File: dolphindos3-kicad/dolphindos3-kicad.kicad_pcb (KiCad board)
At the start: 2 copper layers, 23 parts, among them CN1 MB_CPU, CN2 parallel0, IC1 6502, IC10 74LS08, IC2 27256, IC3 6264, IC4 6821, IC5 74LS08, IC6 74LS08, IC7 74LS32, IC8 74LS04, IC9 74LS32

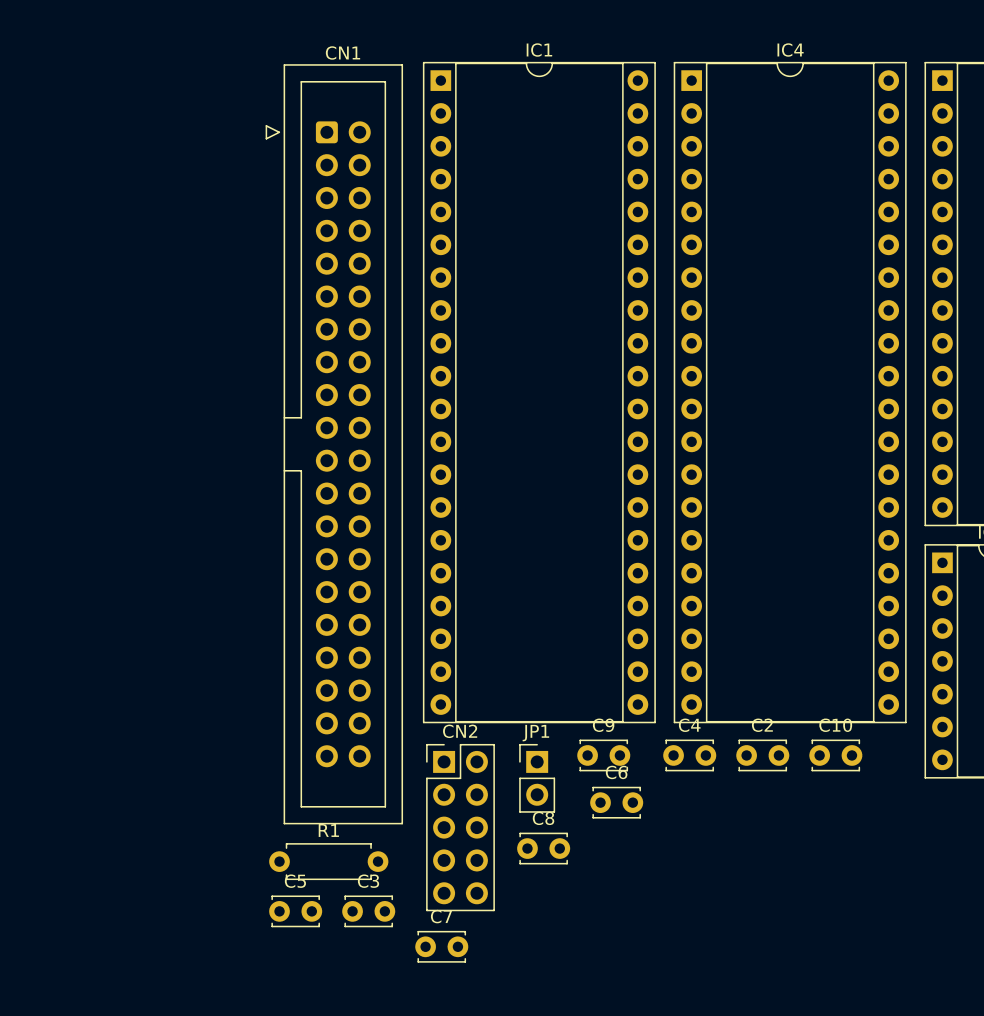
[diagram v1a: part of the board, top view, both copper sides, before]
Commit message: IDC socket for parallel cable, added JP2 for drive reset to match gerbers
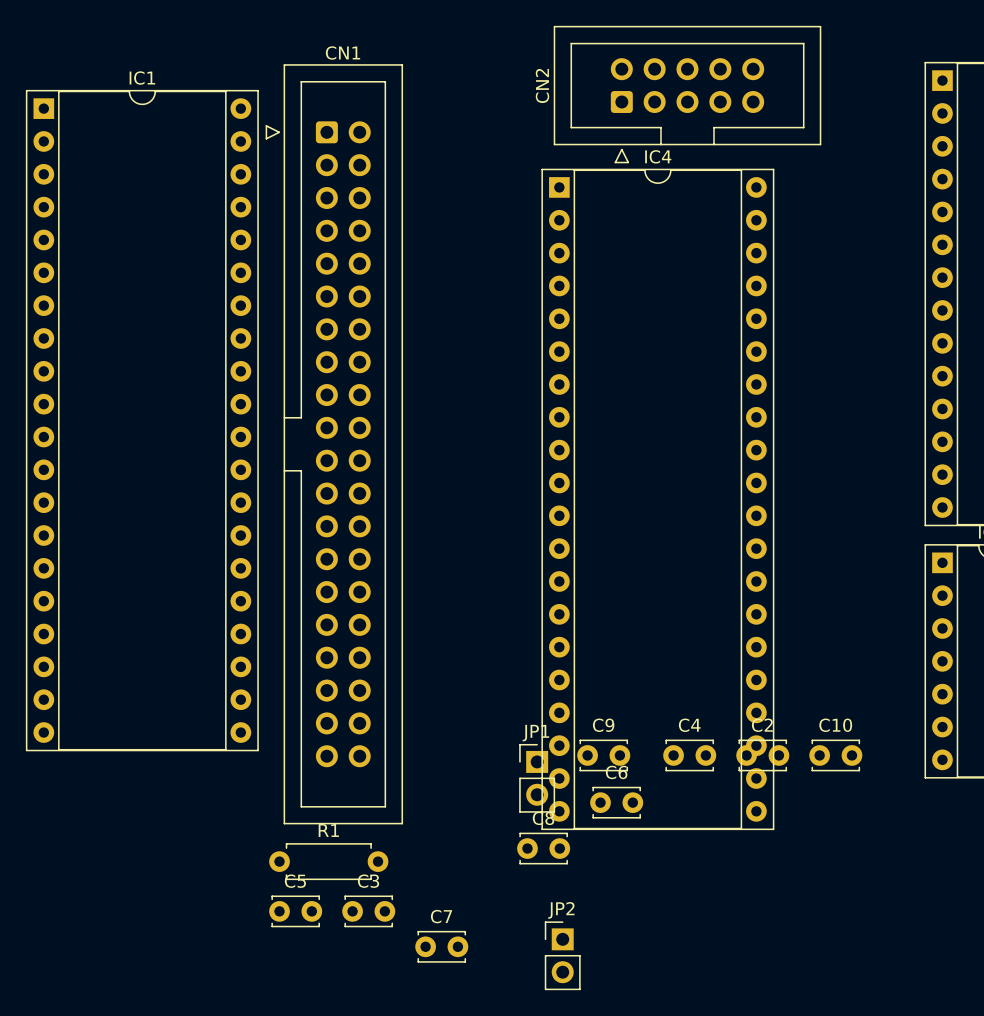
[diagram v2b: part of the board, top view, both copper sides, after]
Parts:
- added JP2: Conn_01x02, Connector_PinHeader_2.54mm:PinHeader_1x02_P2.54mm_Vertical, F.Cu at (190.2, 84.3)
- CN2: footprint Connector_PinHeader_2.54mm:PinHeader_2x05_P2.54mm_Vertical -> Connector_IDC:IDC-Header_2x05_P2.54mm_Vertical
- moved CN2 52.9 mm to (194.8, 19.6), turned to 90 degrees
- moved IC1 30.8 mm to (150.1, 20.1)
- moved IC4 13.2 mm to (190.0, 26.2)

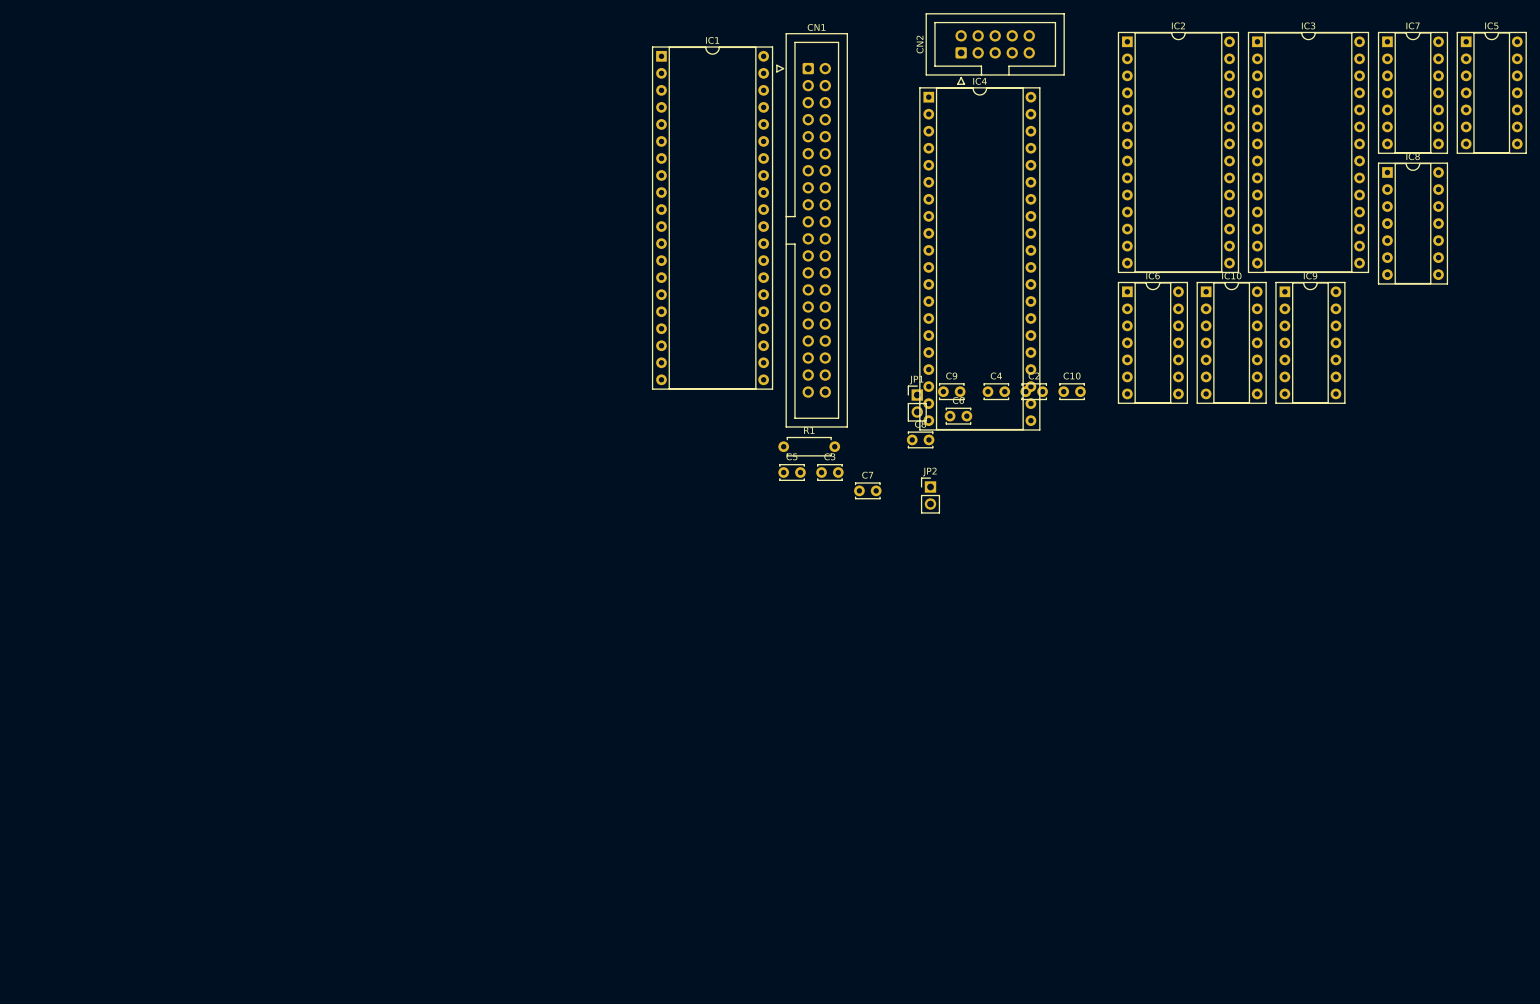
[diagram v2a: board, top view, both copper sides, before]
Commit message: F.Cu, B.Cu and F.Silkscreen copied from SliverDreams! rev2a gerber files, Edge.cuts eyeballed; placed parts and added footprints
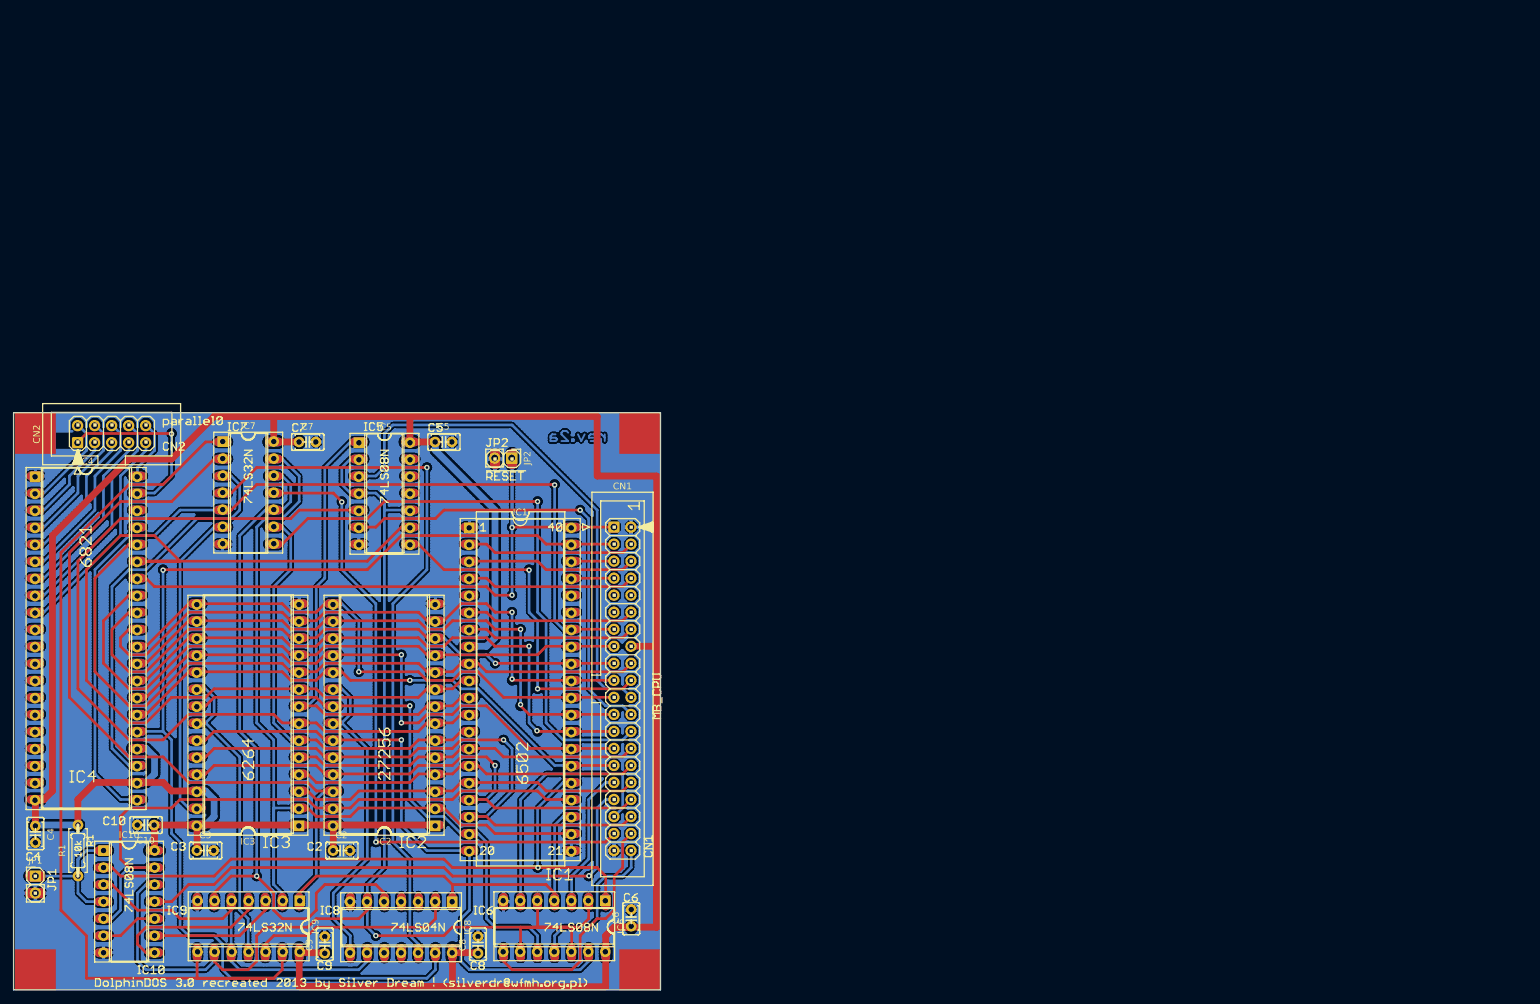
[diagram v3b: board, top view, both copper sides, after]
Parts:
- moved IC3 184.8 mm to (96.0, 134.9), turned to 180 degrees
- moved IC10 184.4 mm to (66.9, 138.6)
- moved IC7 183.7 mm to (84.6, 77.5)
- moved IC8 176.9 mm to (118.9, 146.2), turned to -90 degrees
- moved IC5 175.7 mm to (105.0, 77.7)
- moved IC9 172.8 mm to (96.1, 146.1), turned to -90 degrees
- moved C4 156.2 mm to (56.7, 134.9), turned to -90 degrees
- moved IC2 156.1 mm to (116.3, 134.9), turned to 180 degrees
- moved C10 150.3 mm to (74.4, 134.8), turned to 180 degrees
- moved JP1 149.9 mm to (56.7, 142.4)
- moved IC4 144.9 mm to (56.6, 82.8)
- moved CN2 144.1 mm to (63.0, 77.7)
- moved C9 124.7 mm to (99.9, 153.9), turned to 90 degrees
- moved C2 124.0 mm to (101.1, 138.6)
- moved R1 123.2 mm to (63.1, 142.4), turned to 90 degrees
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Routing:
- net GND: track 0.00 -> 16178.4 mm
- net VCC: track 0.00 -> 610.9 mm
- net Net-(IC10-Pad12): track 0.00 -> 230.4 mm, vias 0 -> 1
- net /A13: track 0.00 -> 190.4 mm
- net /phi2: track 0.00 -> 182.6 mm, vias 0 -> 1
- net /A1: track 0.00 -> 159.9 mm
- net Net-(IC7-Pad1): track 0.00 -> 151.5 mm
- net /R/~{W}: track 0.00 -> 149.9 mm, vias 0 -> 1
- net /A12: track 0.00 -> 145.8 mm
- net /A3: track 0.00 -> 139.9 mm
- net /A0: track 0.00 -> 120.9 mm
- net Net-(IC7-Pad10): track 0.00 -> 115.0 mm, vias 0 -> 1
- net /A15: track 0.00 -> 113.7 mm, vias 0 -> 1
- net Net-(IC7-Pad4): track 0.00 -> 113.4 mm, vias 0 -> 1
- net /~{RESET}: track 0.00 -> 108.1 mm, vias 0 -> 2
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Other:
- board outline added: 96.5 x 86.1 mm

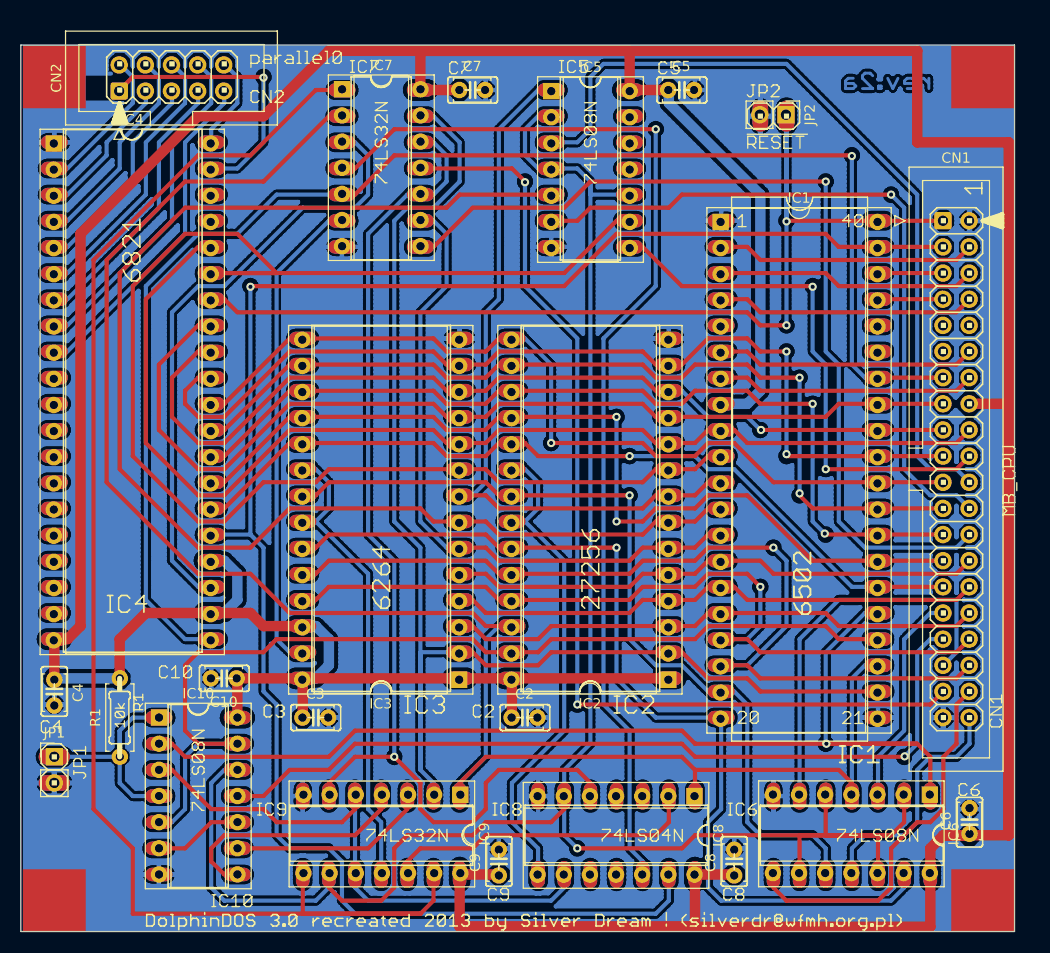
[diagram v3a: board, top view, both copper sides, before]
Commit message: mods: RAM A13/14 from PIA PB, ROM A15, unused gate inputs tied to GND pcb: autorouted, parts moved for C128DCR plug-in option
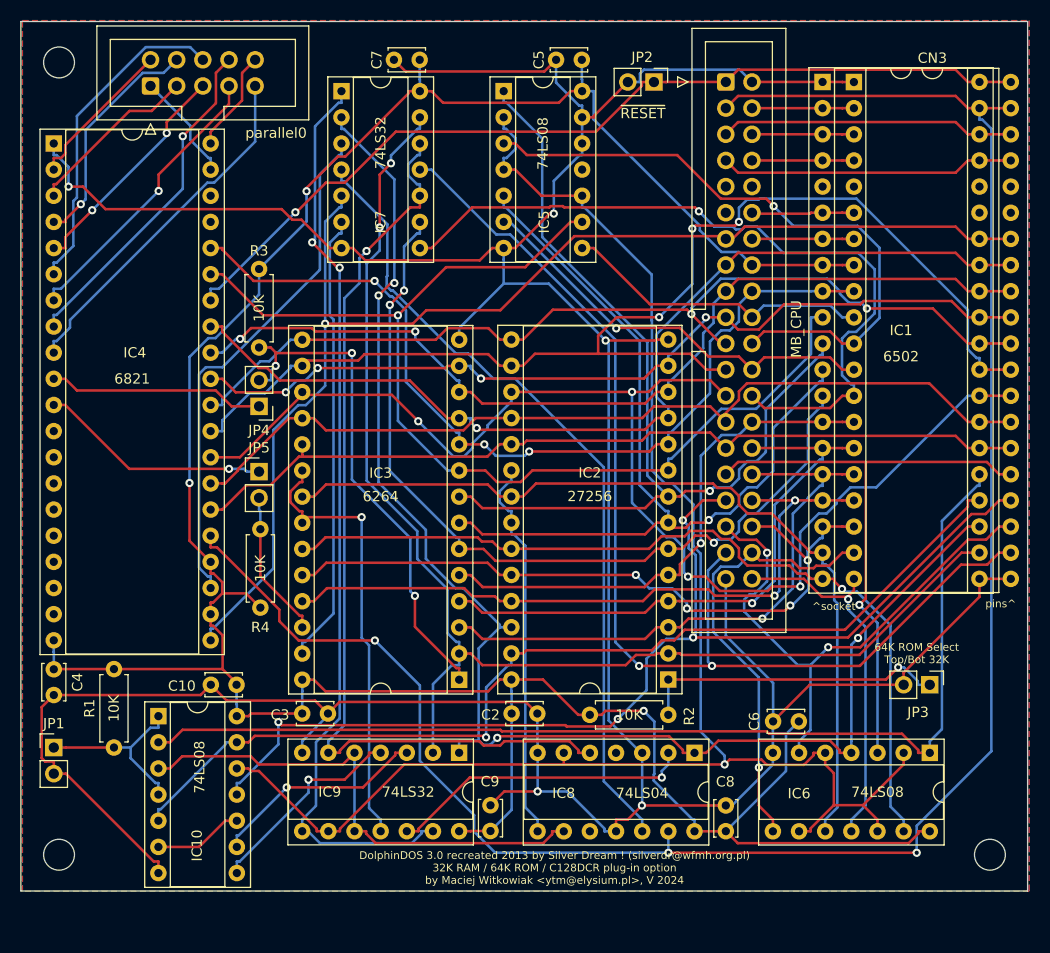
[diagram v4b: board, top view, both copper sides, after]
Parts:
- added CN3: MB_CPU_PINS, Package_DIP:DIP-40_W15.24mm, F.Cu at (134.4, 76.8)
- added H1: MountingHole, MountingHole:MountingHole_3mm, F.Cu at (57.1, 74.9)
- added H3: MountingHole, MountingHole:MountingHole_3mm, F.Cu at (57.1, 151.9)
- added H4: MountingHole, MountingHole:MountingHole_3mm, F.Cu at (147.6, 151.9)
- added JP3: Conn_01x02, Connector_PinHeader_2.54mm:PinHeader_1x02_P2.54mm_Vertical, F.Cu at (141.7, 135.4)
- added JP4: Jumper_2_Open, Connector_PinHeader_2.54mm:PinHeader_1x02_P2.54mm_Vertical, F.Cu at (76.6, 108.3)
- added JP5: Jumper_2_Open, Connector_PinHeader_2.54mm:PinHeader_1x02_P2.54mm_Vertical, F.Cu at (76.6, 114.7)
- added R2: 10K, Resistor_THT:R_Axial_DIN0207_L6.3mm_D2.5mm_P7.62mm_Horizontal, F.Cu at (116.3, 138.3)
- added R3: 10K, Resistor_THT:R_Axial_DIN0207_L6.3mm_D2.5mm_P7.62mm_Horizontal, F.Cu at (76.6, 95.0)
- added R4: 10K, Resistor_THT:R_Axial_DIN0207_L6.3mm_D2.5mm_P7.62mm_Horizontal, F.Cu at (76.7, 127.9)
- moved CN1 25.0 mm to (121.9, 76.8)
- moved C6 19.9 mm to (129.0, 138.9), turned to 180 degrees
- moved IC1 16.8 mm to (131.3, 76.8)
- moved JP2 13.2 mm to (114.9, 76.8)
- moved C5 8.90 mm to (107.9, 74.7), turned to 180 degrees
- moved C7 4.84 mm to (92.2, 74.7), turned to 180 degrees
- moved IC5 4.62 mm to (100.3, 77.7)
- moved C9 4.39 mm to (99.1, 149.6)
- moved C8 4.37 mm to (121.9, 149.6)
- moved IC8 4.20 mm to (118.9, 142.0)
- moved IC9 4.08 mm to (96.0, 142.0)
- moved IC6 4.05 mm to (141.7, 142.0)
- moved CN2 3.09 mm to (66.0, 77.2)
- moved R1 1.06 mm to (62.5, 141.5)
- moved C4 1.02 mm to (56.6, 133.9)
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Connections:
- IC2 pad 1: VCC -> Net-(IC2-Pad1)
- IC3 pad 1: VCC -> /A13_RAM
- IC3 pad 26: VCC -> /A14_RAM
- IC4 pad 10: unconnected-(IC4-Pad10) -> /PB0
- IC4 pad 11: unconnected-(IC4-Pad11) -> /PB1
- IC5 pad 12: unconnected-(IC5-Pad12) -> GND
- IC5 pad 13: unconnected-(IC5-Pad13) -> GND
- IC8 pad 11: unconnected-(IC8-Pad11) -> GND
- IC8 pad 3: unconnected-(IC8-Pad3) -> GND
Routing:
- net GND: track 16178.4 -> 365.6 mm, vias 0 -> 5
- net VCC: track 610.9 -> 271.8 mm, vias 0 -> 3
- net Net-(IC10-Pad12): track 230.4 -> 164.0 mm
- net Net-(IC7-Pad1): track 151.5 -> 90.0 mm, vias 0 -> 2
- net /A1: track 159.9 -> 104.8 mm, vias 0 -> 1
- net /A3: track 139.9 -> 85.1 mm, vias 0 -> 1
- net /A13: track 190.4 -> 140.5 mm, vias 0 -> 4
- net /A13_RAM: track 0.00 -> 49.5 mm, vias 0 -> 3
- net Net-(IC7-Pad4): track 113.4 -> 78.6 mm, vias 1 -> 0
- net (no net): track 34.5 -> 0.00 mm
- net /A15MB: track 23.8 -> 57.9 mm, vias 0 -> 1
- net /A0: track 120.9 -> 86.9 mm, vias 0 -> 3
- net /A3MB: track 71.8 -> 41.0 mm
- net Net-(IC2-Pad1): track 0.00 -> 30.2 mm, vias 0 -> 1
- net /R/~{W}: track 149.9 -> 120.3 mm
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- added copper zone on B.Cu, net GND
- added copper zone on F.Cu, net GND
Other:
- board size 96.5 x 86.1 mm -> 97.8 x 84.5 mm
- board text added: "64K ROM Select Top/Bot 32K"
- board text added: "DolphinDOS 3.0 recreated 2013 by Silver Dream ! (silverdr@wfmh.org.pl) 32K RAM / 64K ROM / C128DCR plug-in option by Maciej Witkowiak <ytm@elysium.pl>, V 2024"
- board text added: "^socket"
- board text added: "pins^"
- board text added: "~{RESET}"
